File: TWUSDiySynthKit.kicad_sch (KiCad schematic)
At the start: 53 parts, among them J1 Conn_02x02_Counter_Clockwise, J10 Conn_01x03_Socket, J2 Conn_01x02, J3 Conn_01x07_Pin, J4 Conn_01x07_Pin, J5 Raspberry_Pi_2x20_PTH, J6 Conn_01x04_Socket, J7 Conn_01x04_Socket, J8 Conn_01x04_Socket, J9 Conn_01x03_Socket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

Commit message: Added p2.54mm dupont headers as alternative for Stemma JST connectors
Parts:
- added J11, J12: Conn_01x03_Socket, Connector_PinSocket_2.54mm:PinSocket_1x03_P2.54mm_Vertical, symbol Connector:Conn_01x03_Socket
- added J14: Conn_01x04_Socket, Connector_PinSocket_2.54mm:PinSocket_1x04_P2.54mm_Vertical, symbol Connector:Conn_01x04_Socket
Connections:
- net +3.3V: now also J11.2 (Pin_2), J12.2 (Pin_2), J14.3 (Pin_3)
- net GND: now also J11.1 (Pin_1), J12.1 (Pin_1), J14.4 (Pin_4)
- net at A1.5 (GPIO3), A2.5 (GPIO3), J5.5 (SCL/GPIO3)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: now also J14.1 (Pin_1)
- net at A1.4 (GPIO2), A2.4 (GPIO2), J5.3 (SDA/GPIO2)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: now also J14.2 (Pin_2)
- net at A1.27 (GPIO21), A2.27 (GPIO21), J10.3 (Pin_3)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: now also J11.3 (Pin_3)
- net at A1.29 (GPIO22), A2.29 (GPIO22), J5.11 (GPIO17)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: now also J12.3 (Pin_3)

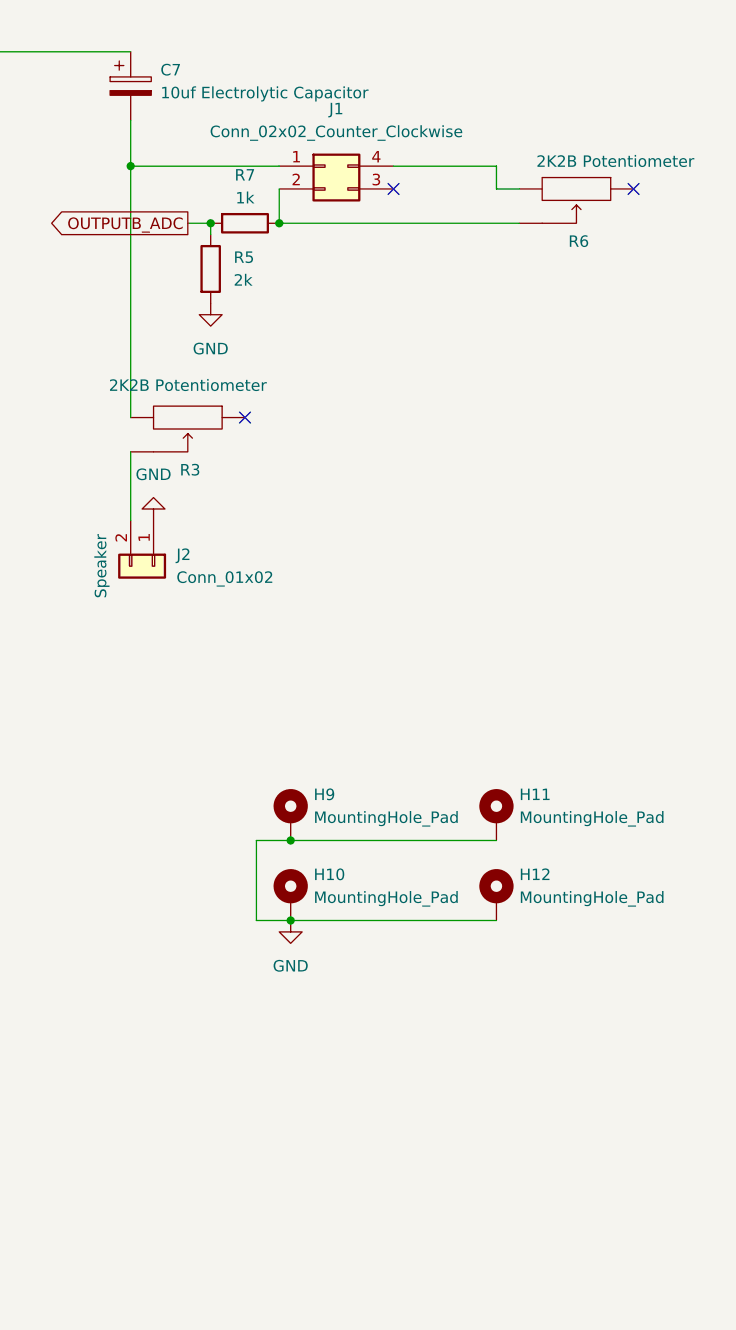
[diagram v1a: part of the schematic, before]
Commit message: Added further guarding traces to reduce EMI, optimised vias etc. etc.
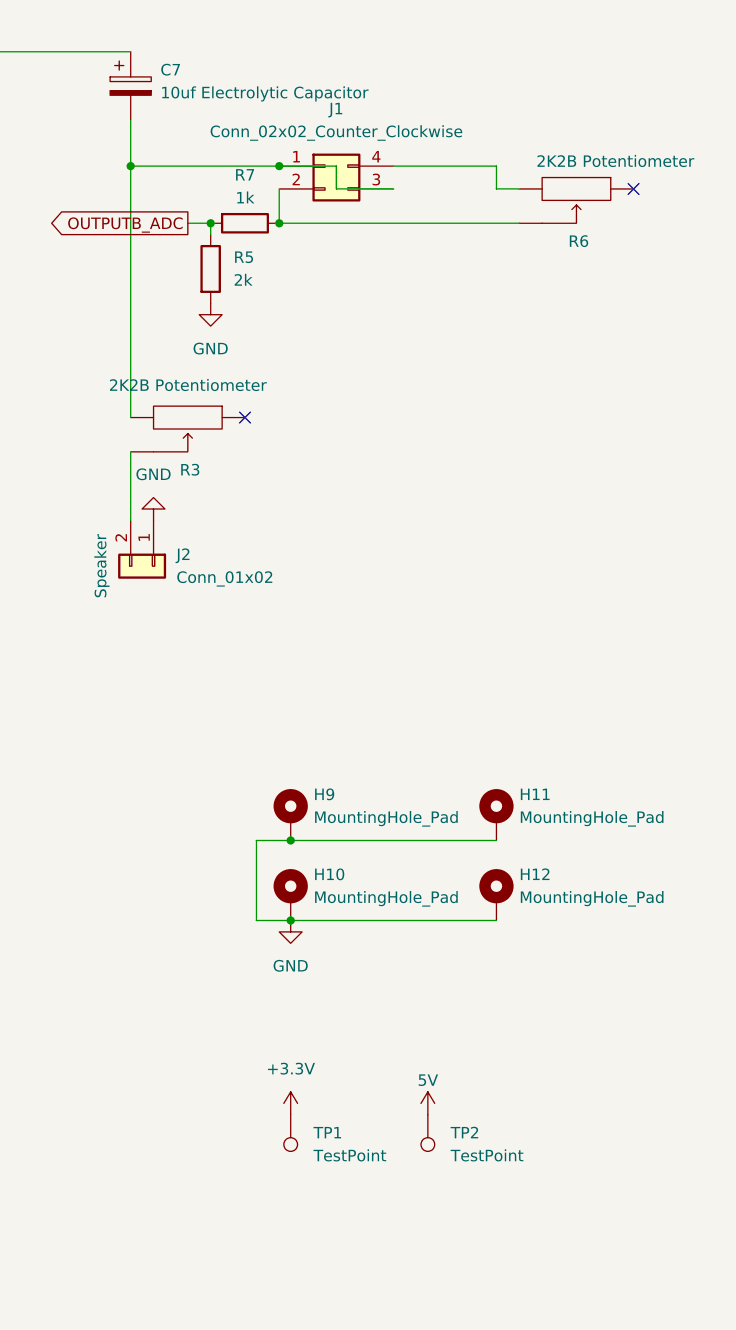
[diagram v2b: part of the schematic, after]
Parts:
- added TP1, TP2: TestPoint, TestPoint:TestPoint_Pad_D2.5mm, symbol Connector:TestPoint
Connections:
- net +3.3V: now also TP1.1
- net 5V: now also TP2.1
- net at C7.2, J1.1 (Pin_1), R3.1: now also J1.3 (Pin_3)
- no-connect marks 8 -> 7

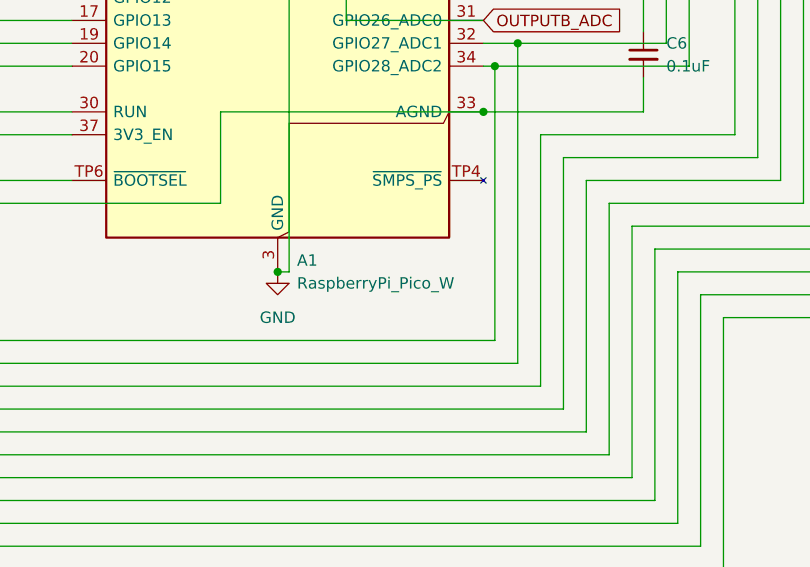
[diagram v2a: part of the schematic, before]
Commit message: Added bill of materials
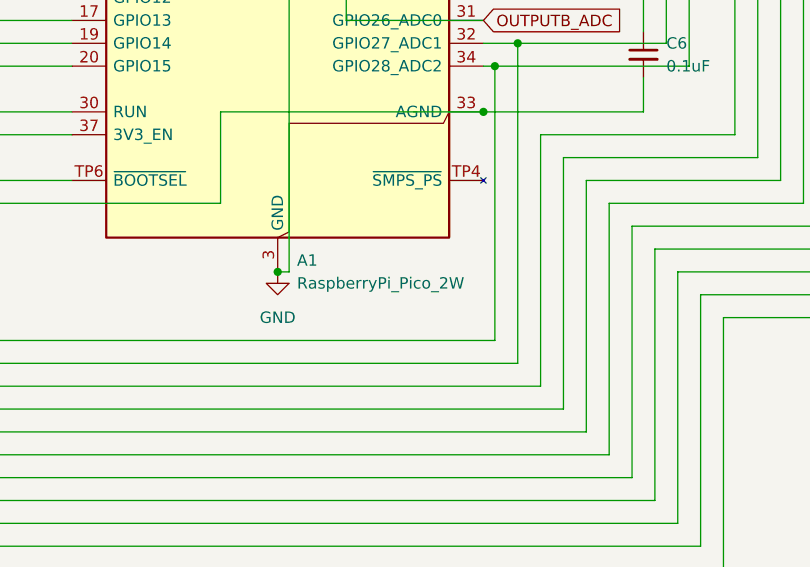
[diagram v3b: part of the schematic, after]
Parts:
- A1: value RaspberryPi_Pico_W -> RaspberryPi_Pico_2W; Manufacturer (none) -> Raspberry Pi Foundation; Manufacturer_Part_Number (none) -> SC1633; Mouser Part Number (none) -> 358-SC1633
- C1, C10, C11, C12, C13, C14, C3, C9: JLCPCB ID (none) -> C6766062; Manufacturer (none) -> Samsung Electro-Mechanics; Manufacturer_Part_Number (none) -> CL31B104KBCNNND; Mouser Part Number (none) -> 187-CL31B104KBCNNND
- C2, C8: JLCPCB ID C57112 -> C16196152; Manufacturer AVX Corporation -> Samsung Electro-Mechanics; Manufacturer_Part_Number (none) -> CL31B103KHFNFNE; Mouser Part Number (none) -> 187-CL31B103KHFNFNE
- C4, C5, C6: JLCPCB ID C14663 -> C6766062; Manufacturer AVX Corporation -> Samsung Electro-Mechanics; Manufacturer_Part_Number (none) -> CL31B104KBCNNND; Mouser Part Number (none) -> 187-CL31B104KBCNNND
- C7: JLCPCB ID (none) -> C1583769; Manufacturer (none) -> Panasonic; Manufacturer_Part_Number (none) -> ECE-A1HKS100B; Mouser Part Number (none) -> 667-ECE-A1HKS100B
- J10, J9: JLCPCB ID (none) -> C157929; Manufacturer (none) -> Japan Solderless Terminals Commercial; Manufacturer_Part_Number (none) -> S3B-PH-K-S(LF)(SN); Mouser Part Number (none) -> 306-S3BPHKSLFSN
- J2: JLCPCB ID (none) -> C157931; Manufacturer (none) -> Japan Solderless Terminals; Manufacturer_Part_Number (none) -> S2B-XH-A(LF)(SN); Mouser Part Number (none) -> 306-S2B-XH-ALFSN
- J6: JLCPCB ID (none) -> C163037; Manufacturer (none) -> Japan Solderless Terminals; Manufacturer_Part_Number (none) -> S4B-XH-A-1(LF)(SN); Mouser Part Number (none) -> 306-S4BXHA1LFSN
- J7: JLCPCB ID (none) -> C157926; Manufacturer (none) -> Japan Solderless Terminals; Manufacturer_Part_Number (none) -> S4B-PH-K-S(LF)(SN); Mouser Part Number (none) -> 306-S4BPHKSLFSN
- J8: JLCPCB ID (none) -> C7279904; Manufacturer (none) -> Japan Solderless Terminals; Manufacturer_Part_Number (none) -> SM04B-GHMG-TB-(LF)(SN); Mouser Part Number (none) -> 306-SM04BGHMGTBLFSN
- R1, R2, R3, R6: JLCPCB ID (none) -> C163036; Manufacturer (none) -> Japan Solderless Terminals; Manufacturer_Part_Number (none) -> S3B-XH-A-1(LF)(SN); Mouser Part Number (none) -> 306-S3BXHA1LFSN
- R4, R7: JLCPCB ID C21190 -> C4130738; Manufacturer Yageo -> SEI Stackpole; Manufacturer_Part_Number (none) -> RMCF0603JG1K00; Mouser Part Number (none) -> 708-RMCF0603JG1K00
- R5: JLCPCB ID C22975 -> C2076992; Manufacturer Yageo -> Vishay; Manufacturer_Part_Number (none) -> M55342E12B2B00RT5; Mouser Part Number (none) -> 75-M55342E12B2B00RT5
- R8, R9: JLCPCB ID C25804 -> C2130614; Manufacturer Yageo -> Vishay; Manufacturer_Part_Number (none) -> TNPW060310K0FHEA; Mouser Part Number (none) -> 71-TNPW060310K0FHEA
- U1: JLCPCB ID (none) -> C66175; Manufacturer (none) -> Texas Instruments; Manufacturer_Part_Number (none) -> NE556N; Mouser Part Number (none) -> 595-NE556N

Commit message: Added PDF file of pcb and schematic
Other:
- company: (none) -> GreeniusGenius
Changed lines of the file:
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@@
 	(generator_version "9.0")
 	(paper "A3")
+	(title_block
+		(company "GreeniusGenius")
+	)
 	(junction
 		(at 20.32 53.34)
